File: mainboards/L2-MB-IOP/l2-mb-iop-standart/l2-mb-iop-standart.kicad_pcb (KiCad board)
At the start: 2 copper layers, 100 x 90 mm, 46 parts, among them J1 URP_Conn_01x12_Socket, J10 GPP_Conn_01x12_Socket, J11 GPP_Conn_01x12_Socket, J12 GPP_Conn_01x12_Socket, J13 GPP_Conn_01x12_Socket, J14 GPP_Conn_01x12_Socket, J15 AIP_Conn_01x12_Socket, J16 AIP_Conn_01x12_Socket, J17 AIP_Conn_01x12_Socket, J18 AIP_Conn_01x12_Socket, J19 ICP_Conn_01x12_Socket, J2 URP_Conn_01x12_Socket, J20 ICP_Conn_01x12_Socket, J21 AIP_Conn_01x12_Socket, J22 AIP_Conn_01x12_Socket, J23 Conn_01x03_Pin, J24 Conn_01x02_Pin, J25 Conn_01x02_Pin, J26 Conn_01x02_Pin, J27 Conn_01x03_Pin, J28 Conn_01x02_Pin, J29 Conn_01x02_Pin, J3 GPP_Conn_01x12_Socket, J4 GPP_Conn_01x12_Socket, J5 GPP_Conn_01x12_Socket, J6 GPP_Conn_01x12_Socket, J7 GPP_Conn_01x12_Socket, J8 GPP_Conn_01x12_Socket, J9 GPP_Conn_01x12_Socket, SW1 SW_SPDT, U1 LM2596s_module, U2 LM2596_mini_module

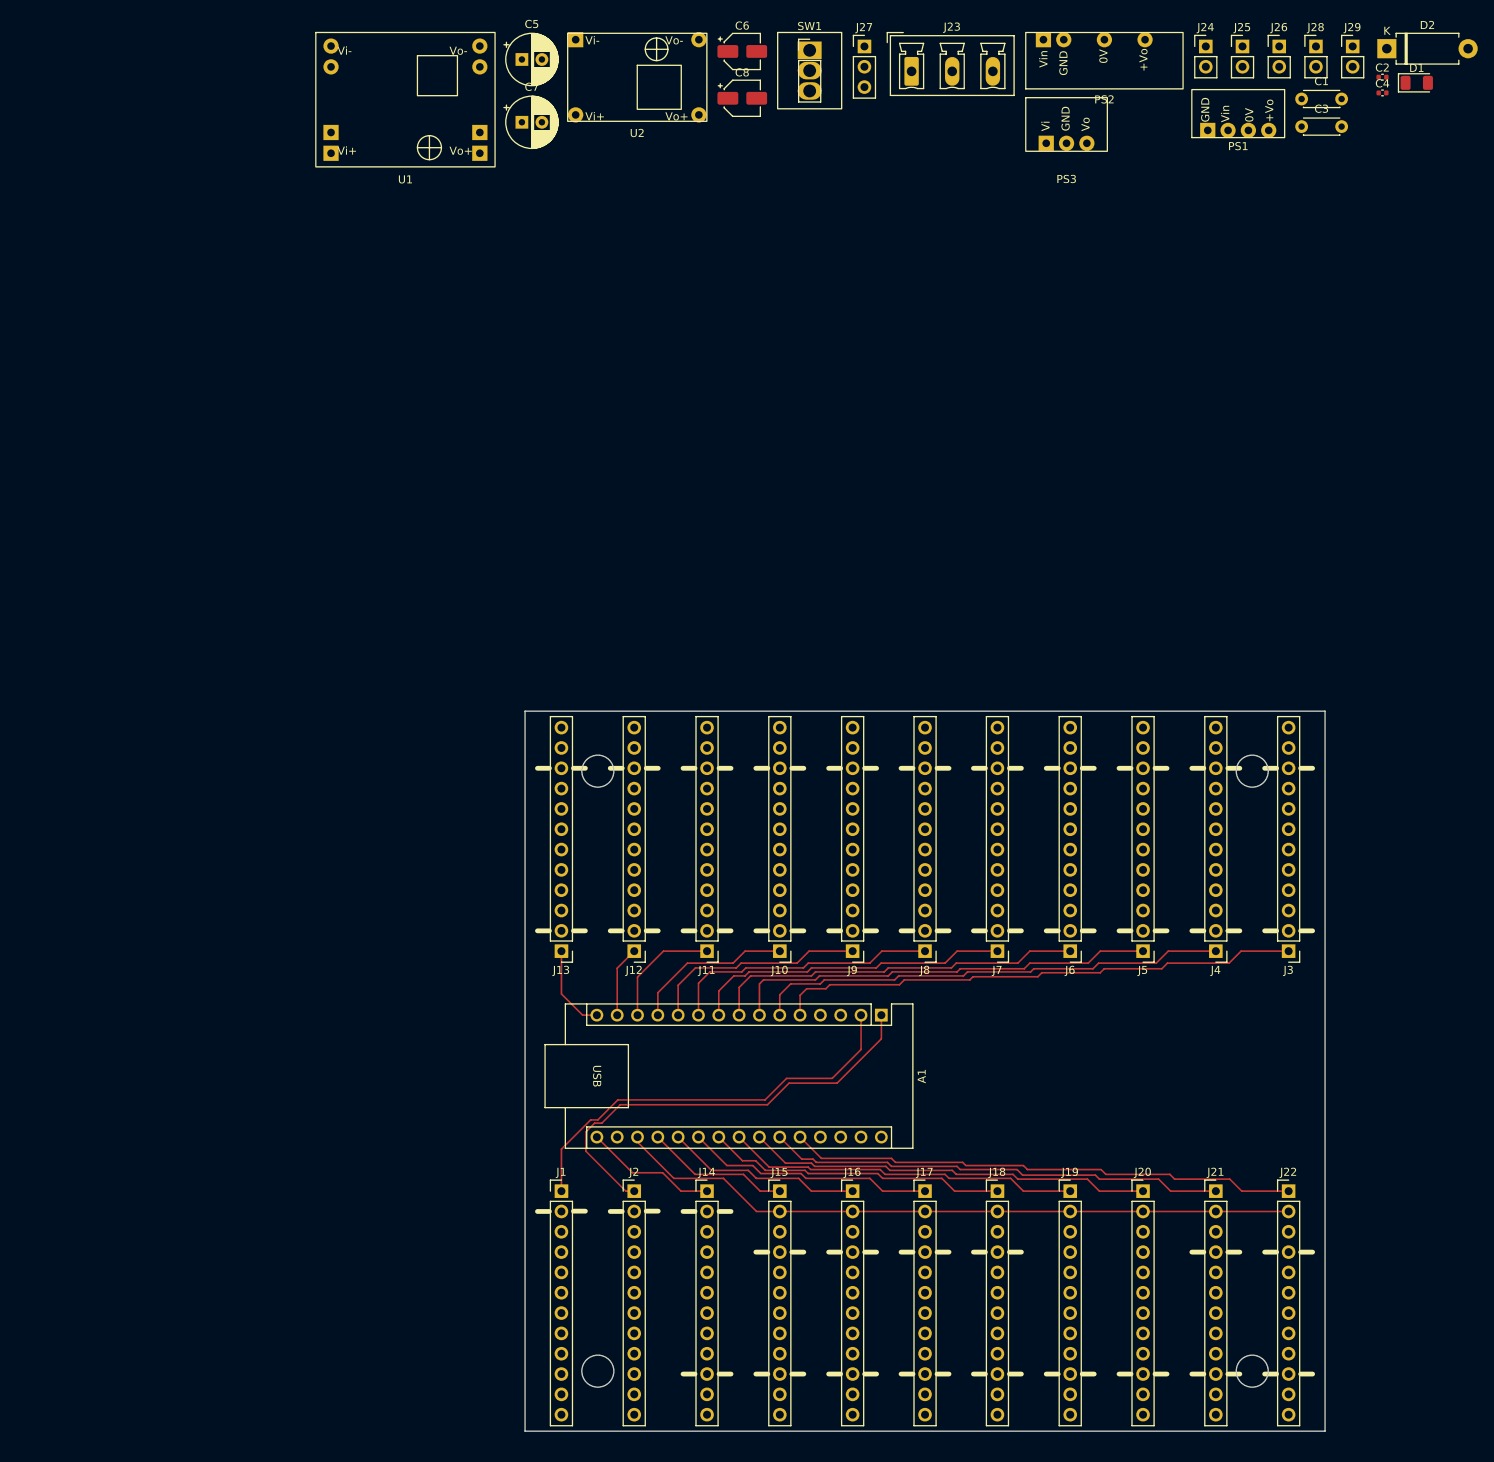
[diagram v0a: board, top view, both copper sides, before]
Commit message: Trying to place all jumpers on board.
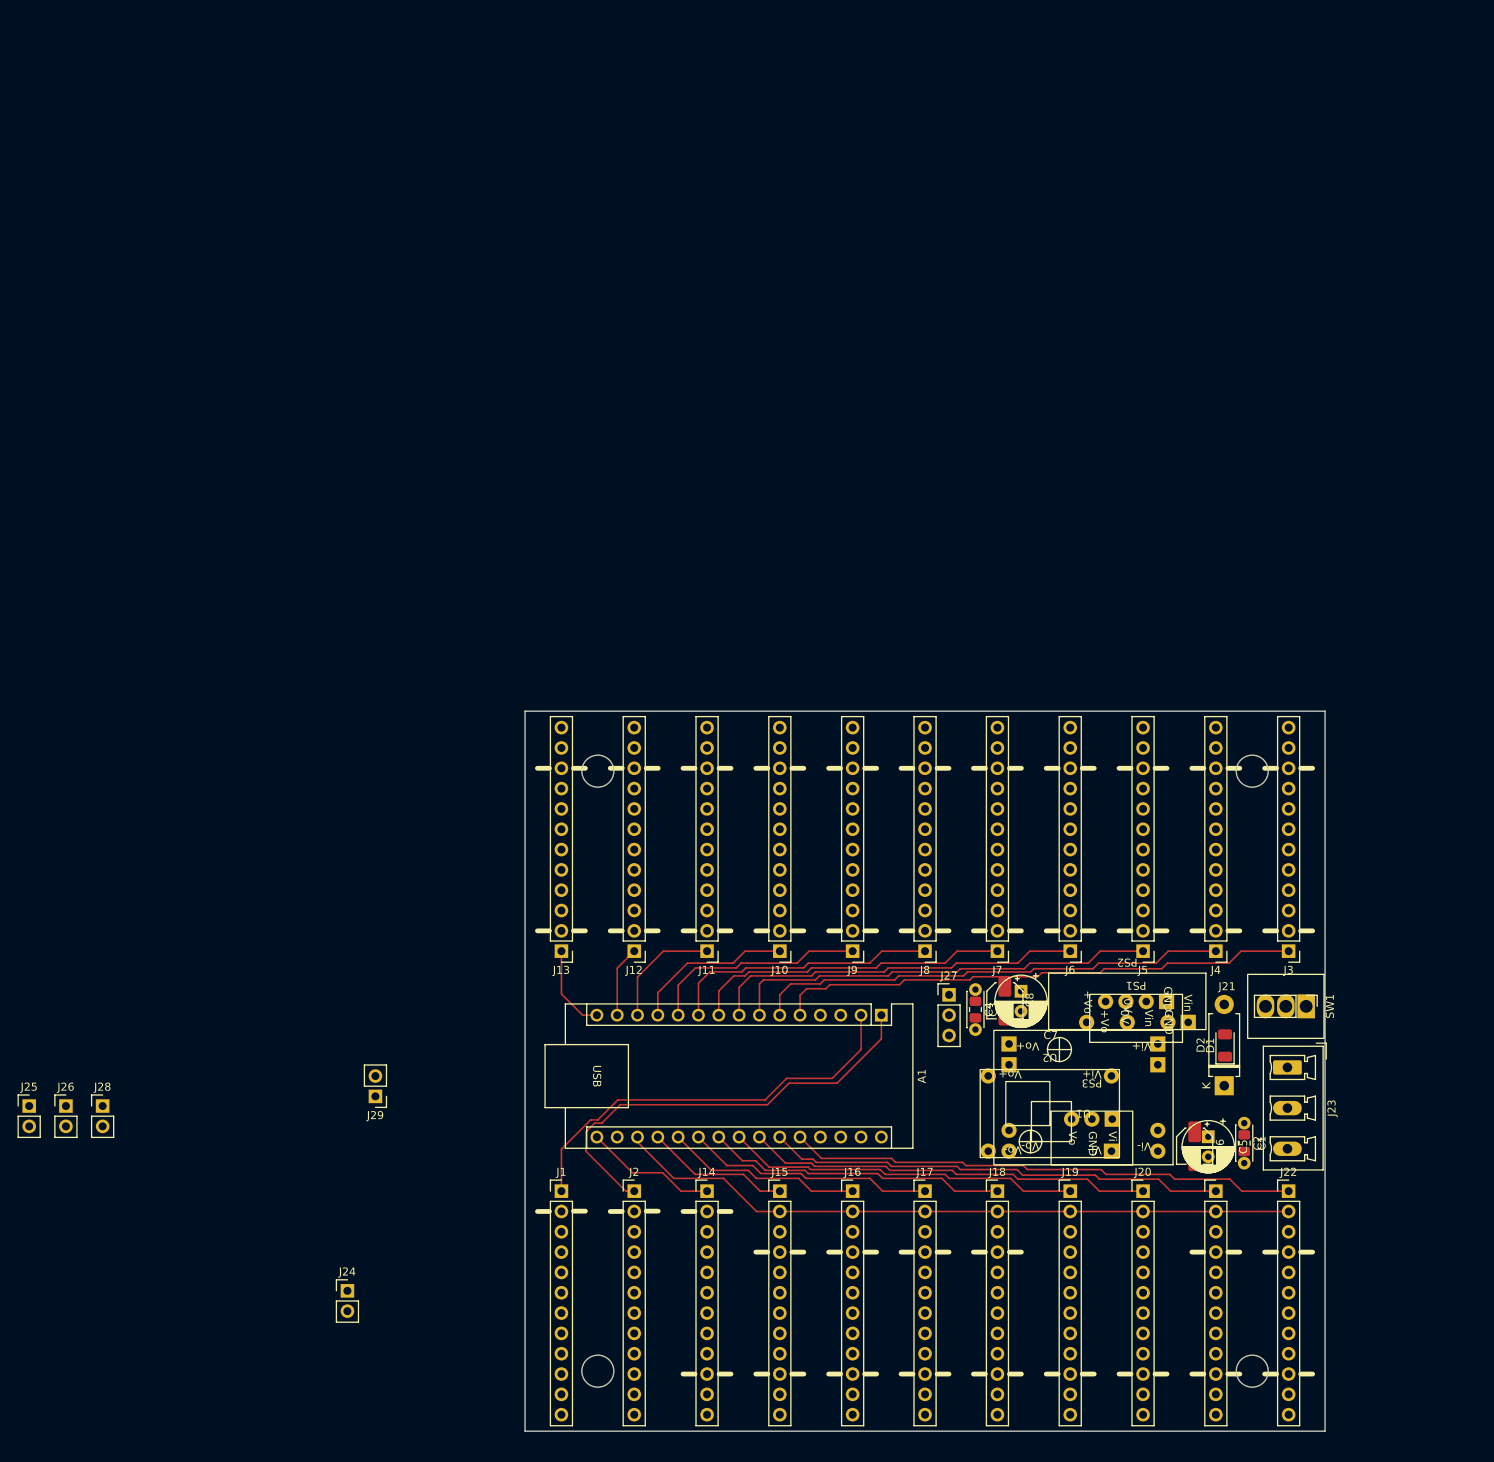
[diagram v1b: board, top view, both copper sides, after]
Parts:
- C2, C4: footprint Capacitor_SMD:C_0402_1005Metric -> Capacitor_SMD:C_0805_2012Metric_Pad1.18x1.45mm_HandSolder
- moved J26 201.4 mm to (42.6, 99.4)
- moved J28 201.4 mm to (47.2, 99.4)
- moved J25 201.4 mm to (38.0, 99.4)
- moved J24 189.0 mm to (77.8, 122.5)
- moved J29 179.3 mm to (81.3, 98.2), turned to 180 degrees
- moved C5 159.7 mm to (185.4, 103.2), turned to -90 degrees
- moved U1 150.8 mm to (169.8, 98.3), turned to 180 degrees
- moved C6 148.1 mm to (183.7, 104.4), turned to -90 degrees
- moved U2 139.4 mm to (165.6, 100.3), turned to 180 degrees
- moved SW1 134.7 mm to (197.6, 86.9), turned to -90 degrees
- moved C2 134.4 mm to (189.9, 104.0), turned to -90 degrees
- moved J23 133.1 mm to (195.3, 94.5), turned to -90 degrees
- moved D2 131.2 mm to (187.4, 96.8), turned to 90 degrees
- moved C1 128.2 mm to (189.9, 101.5), turned to -90 degrees
- moved C4 125.4 mm to (156.3, 87.3), turned to -90 degrees
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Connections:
- U1 pad 1: +24V -> GND
- U1 pad 2: GND -> +24V
- U1 pad 3: +5V -> GND
- U1 pad 4: GND -> +5V
- U2 pad 1: +24V -> GND
- U2 pad 2: GND -> +24V
- U2 pad 3: +5V -> GND
- U2 pad 4: GND -> +5V

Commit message: Trying to place everithing on board
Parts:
- J27: value Conn_01x03_Pin -> Conn_01x02_Pin; footprint Connector_PinHeader_2.54mm:PinHeader_1x03_P2.54mm_Vertical -> Connector_PinHeader_2.54mm:PinHeader_1x02_P2.54mm_Vertical
- moved J25 115.5 mm to (153.1, 89.3), turned to -90 degrees
- moved J26 111.2 mm to (153.0, 85.4), turned to -90 degrees
- moved J28 103.2 mm to (150.4, 97.2), turned to 90 degrees
- moved J24 75.8 mm to (150.5, 100.9), turned to 90 degrees
- moved J29 71.9 mm to (152.9, 104.8), turned to -90 degrees
- moved J27 7.94 mm to (153.0, 93.4), turned to -90 degrees
- moved SW1 0.81 mm to (196.8, 86.8)
- moved C8 0.54 mm to (159.8, 86.7)
- moved C7 0.35 mm to (161.8, 85.3)
- moved C4 0.20 mm to (156.1, 87.3)
- moved C3 0.20 mm to (156.1, 84.8)
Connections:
- A1 pad 3: Net-(J28-Pin_1) -> unconnected-(A1-~{RESET}-Pad3)
- A1 pad 4: GND1 -> unconnected-(A1-GND-Pad4)
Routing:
- net GND: track 0.00 -> 354.2 mm
- net +24V: track 0.00 -> 321.1 mm
- net GND1: track 0.00 -> 261.7 mm
- net /Not_assigned: track 0.00 -> 259.5 mm
- net /+10V_bipolar: track 0.00 -> 254.4 mm
- net /0V_bipolar: track 0.00 -> 205.5 mm
- net /Diag_for_future: track 0.00 -> 181.8 mm
- net /-10V_bipolar: track 0.00 -> 181.8 mm
- net +5V: track 0.00 -> 79.8 mm
- net Net-(A1-3V3): track 0.00 -> 45.7 mm
- net Net-(A1-AREF): track 85.6 -> 126.9 mm
- net Net-(A1-VIN): track 0.00 -> 20.3 mm
- net Net-(J28-Pin_1): track 0.00 -> 14.9 mm
- net Net-(D1-A): track 0.00 -> 8.54 mm
- net Net-(J23-Pin_1): track 0.00 -> 8.15 mm
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
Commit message: Board first version
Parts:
- removed C5, C7: C_Polarized, Capacitor_THT:CP_Radial_D6.3mm_P2.50mm
- removed C6, C8: C_Polarized, Capacitor_SMD:CP_Elec_4x5.3
- removed D2: D_Schottky, Diode_THT:D_DO-15_P10.16mm_Horizontal
- removed the J23 at (195.3, 94.5)
- removed the J24 at (150.5, 100.9)
- removed the J25 at (153.1, 89.3)
- removed the J26 at (153.0, 85.4)
- removed the J27 at (153.0, 93.4)
- removed the J28 at (150.4, 97.2)
- removed the J29 at (152.9, 104.8)
- removed PS3: DD4012SA, tuxmio:DD4012SA
- removed SW1: SW_SPDT, tuxmio:SW-SPDT_1x03_P2.54mm_Vertical
- removed U1: LM2596s_module, tuxmio:LM2596s_module
- removed U2: LM2596_mini_module, tuxmio:LM2596_mini_module
- added J1: Conn_01x03_Pin, Connector_PinHeader_2.54mm:PinHeader_1x03_P2.54mm_Vertical, F.Cu at (197.9, 85.6)
- added J10: Conn_01x01_Pin, Connector_PinHeader_1.00mm:PinHeader_1x01_P1.00mm_Vertical, F.Cu at (152.3, 88.8)
- added J11: Conn_01x01_Pin, Connector_PinHeader_1.00mm:PinHeader_1x01_P1.00mm_Vertical, F.Cu at (152.3, 86.7)
- added J12: Conn_01x01_Pin, Connector_PinHeader_1.00mm:PinHeader_1x01_P1.00mm_Vertical, F.Cu at (150.0, 88.8)
- added J13: Conn_01x01_Pin, Connector_PinHeader_1.00mm:PinHeader_1x01_P1.00mm_Vertical, F.Cu at (150.0, 102.5)
- added J2: Conn_01x01_Pin, Connector_PinHeader_1.00mm:PinHeader_1x01_P1.00mm_Vertical, F.Cu at (174.6, 84.2)
- added J3: Conn_01x01_Pin, Connector_PinHeader_1.00mm:PinHeader_1x01_P1.00mm_Vertical, F.Cu at (174.6, 90.5)
- added J4: Conn_01x01_Pin, Connector_PinHeader_1.00mm:PinHeader_1x01_P1.00mm_Vertical, F.Cu at (165.9, 90.5)
- added J5: Conn_01x01_Pin, Connector_PinHeader_1.00mm:PinHeader_1x01_P1.00mm_Vertical, F.Cu at (165.9, 86.8)
- added J6: Conn_01x01_Pin, Connector_PinHeader_1.00mm:PinHeader_1x01_P1.00mm_Vertical, F.Cu at (157.1, 88.8)
- added J7: Conn_01x01_Pin, Connector_PinHeader_1.00mm:PinHeader_1x01_P1.00mm_Vertical, F.Cu at (157.4, 105.5)
- added J8: Conn_01x01_Pin, Connector_PinHeader_1.00mm:PinHeader_1x01_P1.00mm_Vertical, F.Cu at (154.8, 90.5)
- added J9: Conn_01x01_Pin, Connector_PinHeader_1.00mm:PinHeader_1x01_P1.00mm_Vertical, F.Cu at (154.8, 85.5)
- C1, C3: footprint Capacitor_THT:C_Disc_D4.3mm_W1.9mm_P5.00mm -> Capacitor_SMD:C_0805_2012Metric_Pad1.18x1.45mm_HandSolder
- C2, C4: value C -> C_Polarized; footprint Capacitor_SMD:C_0805_2012Metric_Pad1.18x1.45mm_HandSolder -> Capacitor_SMD:CP_Elec_4x5.3
- PS2: value B240XS-2W -> DD4012SA; footprint tuxmio:B240XS-2W -> tuxmio:DD4012SA
- moved C3 17.1 mm to (173.0, 87.4), turned to 90 degrees
- moved C2 15.7 mm to (189.1, 88.3)
- moved C1 13.8 mm to (193.7, 88.2), turned to 0 degrees
- moved C4 13.4 mm to (169.5, 87.4), turned to 90 degrees
- moved D1 8.84 mm to (193.8, 85.6), turned to 0 degrees
- moved PS2 5.19 mm to (180.4, 89.8)
- moved PS1 4.73 mm to (181.1, 86.6)
- renumbered J1 to J14, J2 to J15, J3 to J16, J4 to J17, J5 to J18, J6 to J19, J7 to J20, J8 to J21, J9 to J22, J10 to J23, J11 to J24, J12 to J25, J13 to J26, J14 to J27, J15 to J28, J16 to J29, J17 to J30, J18 to J31, J19 to J32, J20 to J33, J21 to J34, J22 to J35
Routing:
- net GND: track 354.2 -> 12.4 mm
- net /-10V_bipolar: track 181.8 -> 241.7 mm
- net /Diag_for_future: track 181.8 -> 234.5 mm
- net /0V_bipolar: track 205.5 -> 249.7 mm
- net Net-(A1-AREF): track 126.9 -> 95.5 mm
- net +5V: track 79.8 -> 52.3 mm
- net +24V: track 321.1 -> 297.8 mm, vias 0 -> 1
- net Net-(A1-VIN): track 20.3 -> 5.77 mm
- net GND1: track 261.7 -> 272.6 mm
- net Net-(J23-Pin_1): track 8.15 -> 0.00 mm
- net Net-(J8-Pin_1): track 14.9 -> 22.3 mm
- net Net-(D1-A): track 8.54 -> 2.71 mm
- net /+10V_bipolar: track 254.4 -> 251.0 mm
- net Net-(A1-3V3): track 45.7 -> 49.0 mm
- added copper zone on B.Cu, net GND
- added copper zone on F.Cu, net GND
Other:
- board text removed: "Top coordinates: 104.55 80 bottom 104.55 110"

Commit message: Started first DO board
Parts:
- J14, J15: footprint tuxmio:MB_URP_socket_PinHeader_1x12_P2.54mm_Vertical -> tuxmio:MB_URP_PinSocket_1x12_P2.54mm_Vertical
- J16, J17, J18, J19, J20, J21, J22, J23, J24, J25, J26, J27: footprint tuxmio:MB_GPP_socket_PinHeader_1x12_P2.54mm_Vertical -> tuxmio:MB_GPP_PinSocket_1x12_P2.54mm_Vertical
- J28, J29, J30, J31, J34, J35: footprint tuxmio:MB_AIP_socket_PinHeader_1x12_P2.54mm_Vertical -> tuxmio:MB_AIP_PinSocket_1x12_P2.54mm_Vertical
- J32, J33: footprint tuxmio:MB_ICP_socket_PinHeader_1x12_P2.54mm_Vertical -> tuxmio:MB_ICP_PinSocket_1x12_P2.54mm_Vertical
